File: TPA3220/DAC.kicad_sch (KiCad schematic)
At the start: 1 part, among them U3 PCM5242RHBR

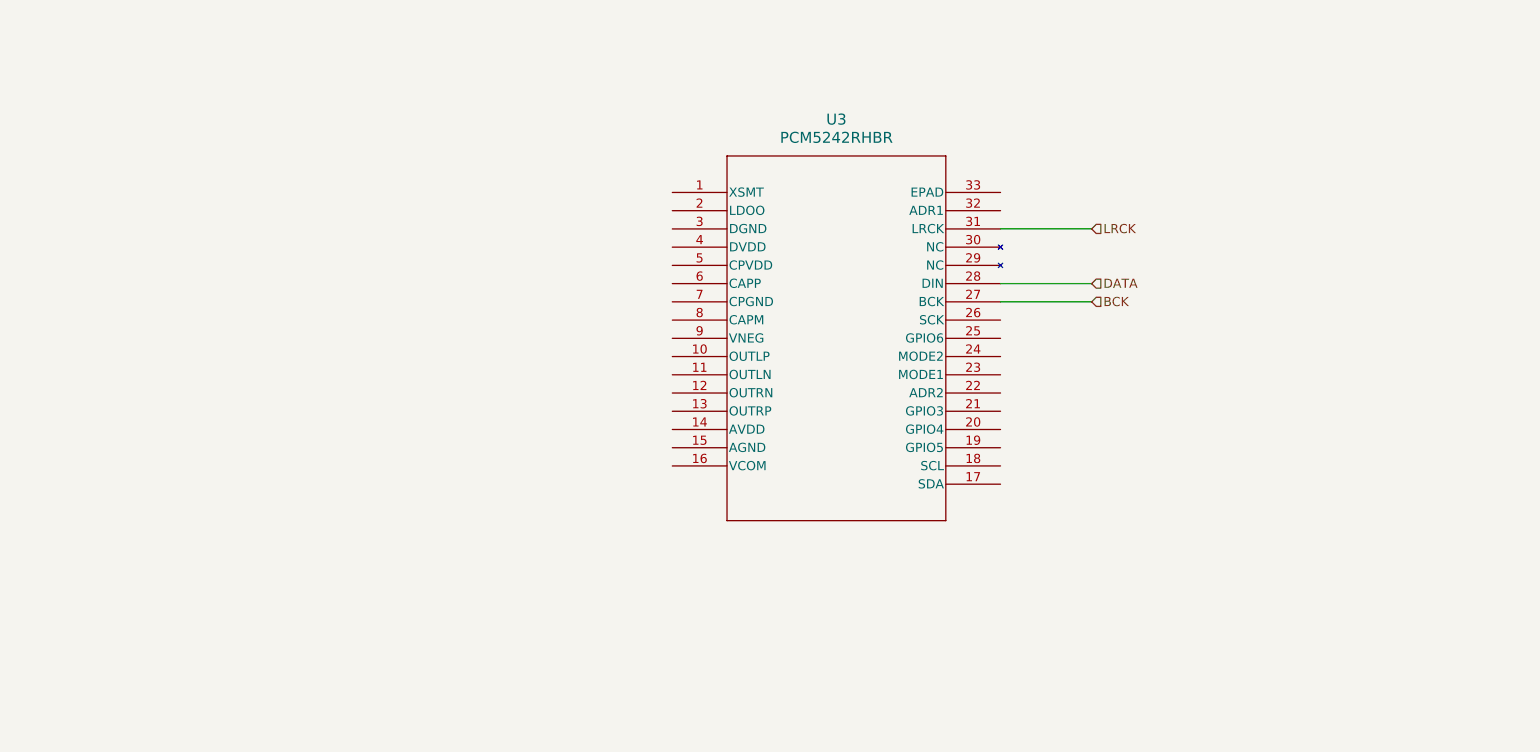
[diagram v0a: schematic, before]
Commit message: TPA3220: snapshot before agent schematic completion
Co-Authored-By: Claude Opus 5.5 <noreply@anthropic.com>
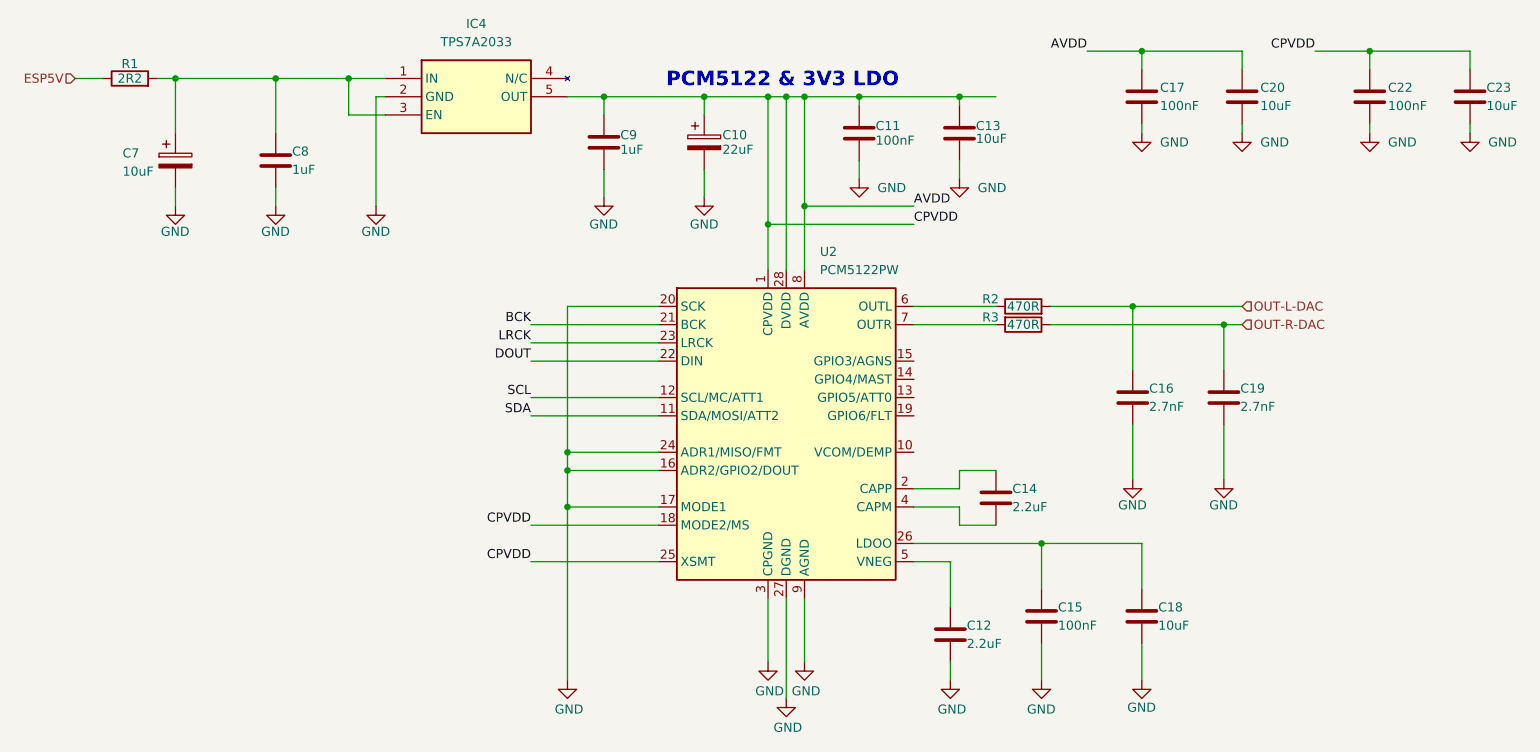
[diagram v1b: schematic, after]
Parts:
- removed U3: PCM5242RHBR, Custom:PCM5242, symbol Custom:PCM5242RHBR
- added C10: 22uF, Capacitor_THT:CP_Radial_D5.0mm_P2.50mm, symbol Device:C_Polarized
- added C11, C15, C17, C22: 100nF, Capacitor_SMD:C_1206_3216Metric_Pad1.33x1.80mm_HandSolder, symbol Device:C
- added C12, C14: 2.2uF, Capacitor_SMD:C_0805_2012Metric_Pad1.18x1.45mm_HandSolder, symbol Device:C
- added C13, C20, C23: 10uF, Capacitor_SMD:C_0805_2012Metric_Pad1.18x1.45mm_HandSolder, symbol Device:C
- added C16, C19: 2.7nF, Capacitor_SMD:C_0805_2012Metric_Pad1.18x1.45mm_HandSolder, symbol Device:C
- added C18: 10uF, Capacitor_SMD:C_1206_3216Metric_Pad1.33x1.80mm_HandSolder, symbol Device:C
- added C7: 10uF, Capacitor_THT:CP_Radial_D4.0mm_P1.50mm, symbol Device:C_Polarized
- added C8, C9: 1uF, Capacitor_SMD:C_1206_3216Metric_Pad1.33x1.80mm_HandSolder, symbol Device:C
- added IC4: TPS7A2033, Custom:SOT95P280X145-5N, symbol Custom:TPS7A2033PDBVR
- added R1: 2R2, Resistor_SMD:R_0805_2012Metric_Pad1.20x1.40mm_HandSolder, symbol Device:R
- added R2, R3: 470R, Resistor_SMD:R_0805_2012Metric_Pad1.20x1.40mm_HandSolder, symbol Device:R
- added U2: PCM5122PW, Package_SO:TSSOP-28_4.4x9.7mm_P0.65mm, symbol Audio:PCM5122PW
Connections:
- net BCK: now also U2.21 (BCK)
- net LRCK: now also U2.23 (LRCK)
- new net: C15.1, C18.1, U2.26 (LDOO)
- new net: C12.1, U2.5 (VNEG)
- new net: R3.2, U2.7 (OUTR)
- new net: C7.1, C8.1, IC4.1 (IN), IC4.3 (EN), R1.2
- new net: C14.1, U2.2 (CAPP)
- new net: C14.2, U2.4 (CAPM)
- new net: R2.1, U2.6 (OUTL)
- new net AVDD: C10.1, C11.1, C13.1, C17.1, C20.1, C22.1, C23.1, C9.1, IC4.5 (OUT), U2.1 (CPVDD), U2.18 (MODE2/MS), U2.25 (XSMT), U2.28 (DVDD), U2.8 (AVDD)
- new net DOUT: U2.22 (DIN)
- new net ESP5V: R1.1
- new net GND: C10.2, C11.2, C12.2, C13.2, C15.2, C16.2, C17.2, C18.2, C19.2, C20.2, C22.2, C23.2, C7.2, C8.2, C9.2, IC4.2 (GND), U2.16 (ADR2/GPIO2/DOUT), U2.17 (MODE1), U2.20 (SCK), U2.24 (ADR1/MISO/FMT), U2.27 (DGND), U2.3 (CPGND), U2.9 (AGND)
- new net OUT-L-DAC: C16.1, R2.2
- new net OUT-R-DAC: C19.1, R3.1
- new net SCL: U2.12 (SCL/MC/ATT1)
- new net SDA: U2.11 (SDA/MOSI/ATT2)
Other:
- note added: "PCM5122 & 3V3 LDO"
